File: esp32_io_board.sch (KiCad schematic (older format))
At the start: 59 parts

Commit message: power pins added on txb104
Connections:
- net +3V3: now also U?.14 (VCCB)
- net +5V: now also U?.1 (VCCA)
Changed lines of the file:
@@
 Text Label 7500 3300 0    50   ~ 0
 RESET
+Wire Wire Line
+	6250 4950 6250 4650
+Wire Wire Line
+	6450 4950 6450 4650
+$Comp
+L power:+3.3V #PWR?
+U 1 1 5CB3F95E
+P 6450 4650
+F 0 "#PWR?" H 6450 4500 50  0001 C CNN
+F 1 "+3.3V" H 6465 4823 50  0000 C CNN
+F 2 "" H 6450 4650 50  0001 C CNN
+F 3 "" H 6450 4650 50  0001 C CNN
+	1    6450 4650
+	1    0    0    -1
+$EndComp
+$Comp
+L power:+5V #PWR?
+U 1 1 5CB41F95
+P 6250 4650
+F 0 "#PWR?" H 6250 4500 50  0001 C CNN
+F 1 "+5V" H 6265 4823 50  0000 C CNN
+F 2 "" H 6250 4650 50  0001 C CNN
+F 3 "" H 6250 4650 50  0001 C CNN
+	1    6250 4650
+	1    0    0    -1
+$EndComp
 $EndSCHEMATC

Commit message: cvpcb
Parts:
- C1, C11, C2, C3, C4, C5, C6, C7, C8: renamed from C?; footprint (none) -> Capacitor_SMD:C_0603_1608Metric
- C10: renamed from C?; footprint (none) -> Capacitor_SMD:CP_Elec_4x4.5
- C9: renamed from C?; footprint (none) -> Capacitor_SMD:CP_Elec_4x5.3
- D1: renamed from D?; footprint (none) -> Diode_SMD:D_SOD-123F
- D2: renamed from D?; footprint (none) -> Diode_SMD:D_SOD-323F
- D3, D6, D7: renamed from D?; footprint (none) -> LED_SMD:LED_RGB_5050-6
- D4, D5: renamed from D?; footprint (none) -> LED_SMD:LED_0603_1608Metric
- F1: renamed from F?; footprint (none) -> Fuse:Fuse_1812_4532Metric_Pad1.30x3.40mm_HandSolder
- J1: renamed from J?; footprint (none) -> Connector_USB:USB_Micro-B_Amphenol_10103594-0001LF_Horizontal
- J10, J2: renamed from J?; footprint (none) -> Connector_PinHeader_2.54mm:PinHeader_2x04_P2.54mm_Vertical
- J11, J12, J13, J14, J15, J16, J17, J18, J3, J6, J7, J8, J9: renamed from J?; footprint (none) -> Connector_PinHeader_2.54mm:PinHeader_1x02_P2.54mm_Vertical
- J4: renamed from J?; footprint (none) -> Connector_PinHeader_2.54mm:PinHeader_1x04_P2.54mm_Vertical
- J5: renamed from J?; value Conn_01x02 -> i2c; footprint (none) -> Connector_PinHeader_2.54mm:PinHeader_1x02_P2.54mm_Vertical
- JP1, JP2, JP3: renamed from JP?; footprint (none) -> Jumper:SolderJumper-2_P1.3mm_Open_RoundedPad1.0x1.5mm
- R1, R10, R11, R2, R3, R4, R5, R6, R7, R8, R9: renamed from R?; footprint (none) -> Resistor_SMD:R_0603_1608Metric
- SW1, SW2: renamed from SW?; footprint (none) -> Button_Switch_SMD:SW_SPST_EVPBF
- U5: renamed from U?; footprint (none) -> Package_TO_SOT_SMD:SOT-223
- gave numbers to parts that had none: 5

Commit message: initial layout without traces
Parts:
- D2: footprint Diode_SMD:D_SOD-323F -> Diode_SMD:D_SOD-123F
- D7: footprint LED_SMD:LED_RGB_5050-6 -> LED_SMD:LED_0603_1608Metric
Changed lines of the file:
@@
 F 0 "D2" V 4500 4200 50  0000 L CNN
 F 1 "D_TVS" V 4650 4150 50  0000 L CNN
-F 2 "Diode_SMD:D_SOD-323F" H 4500 4100 50  0001 C CNN
+F 2 "Diode_SMD:D_SOD-123F" H 4500 4100 50  0001 C CNN
 F 3 "~" H 4500 4100 50  0001 C CNN
 	1    4500 4100
@@
 F 0 "D7" H 12792 6445 50  0000 C CNN
 F 1 "LED" H 12792 6536 50  0000 C CNN
-F 2 "LED_SMD:LED_RGB_5050-6" H 12800 6700 50  0001 C CNN
+F 2 "LED_SMD:LED_0603_1608Metric" H 12800 6700 50  0001 C CNN
 F 3 "~" H 12800 6700 50  0001 C CNN
 	1    12800 6700

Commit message: redesign
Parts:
- removed J10: Conn_02x04_Counter_Clockwise, Connector_PinHeader_2.54mm:PinHeader_2x04_P2.54mm_Vertical, symbol Connector_Generic:Conn_02x04_Counter_Clockwise
- removed J5: i2c, Connector_PinHeader_2.54mm:PinHeader_1x02_P2.54mm_Vertical, symbol Connector_Generic:Conn_01x02
- removed J6, J8, J9: Conn_01x02, Connector_PinHeader_2.54mm:PinHeader_1x02_P2.54mm_Vertical, symbol Connector_Generic:Conn_01x02
- added J?: RASPBERRYPI-40-PIN-GPIO, 2X20-SHROUDED, symbol SparkFun-Boards:RASPBERRYPI-40-PIN-GPIO
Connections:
- net GND: now also J?.14 (GND), J?.20 (GND), J?.25 (GND), J?.30 (GND), J?.34 (GND), J?.39 (GND), J?.6 (GND), J?.9 (GND)
- net at U4.21 (SDO): no longer U6.23 (SDA)
- net at U4.22 (SD1): no longer U6.22 (SCL)
- net at U4.23 (IO15): now also U6.23 (SDA)
- net at U4.24 (IO2): now also U6.22 (SCL)
- net rx: now reaches U4.27 (IO16)
- net rx: now also J?.8 (TXO)
- net tx: now reaches U4.28 (IO17)
- net tx: now also J?.10 (RXI)
- net cs: now reaches U4.29 (IO5)
- net cs: now also J?.24 (CE0)
- net clk: now reaches U4.30 (IO18)
- net clk: now also J?.23 (SCLK)
- net miso: now reaches U4.31 (IO19)
- net miso: now also J?.21 (MISO)
- net sda0: now reaches U4.33 (IO21)
- net sda0: now also J?.3 (SDA)
- net scl0: now reaches U4.36 (IO22)
- net scl0: now also J?.5 (SCL)
- net mosi: now reaches U4.37 (IO23)
- net mosi: now also J?.19 (MOSI)
- no-connect marks 14 -> 37
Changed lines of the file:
@@
 Wire Wire Line
 	9150 6950 9150 7100
-$Comp
-L Connector_Generic:Conn_01x02 J6
-U 1 1 5C5742E1
-P 11150 7150
-F 0 "J6" H 11230 7142 50  0000 L CNN
-F 1 "Conn_01x02" H 11230 7051 50  0000 L CNN
-F 2 "Connector_PinHeader_2.54mm:PinHeader_1x02_P2.54mm_Vertical" H 11150 7150 50  0001 C CNN
-F 3 "~" H 11150 7150 50  0001 C CNN
-	1    11150 7150
-	1    0    0    -1
-$EndComp
-$Comp
-L Connector_Generic:Conn_01x02 J5
-U 1 1 5C5EE2B6
-P 9950 8050
-F 0 "J5" V 9823 8130 50  0000 L CNN
-F 1 "i2c" V 10100 7950 50  0000 L CNN
-F 2 "Connector_PinHeader_2.54mm:PinHeader_1x02_P2.54mm_Vertical" H 9950 8050 50  0001 C CNN
-F 3 "~" H 9950 8050 50  0001 C CNN
-	1    9950 8050
-	0    1    1    0
-$EndComp
-Wire Wire Line
-	9850 6950 9850 7850
-Wire Wire Line
-	9950 6950 9950 7850
-Wire Wire Line
-	10250 6950 10250 7850
-Wire Wire Line
-	10350 6950 10350 7750
 Wire Wire Line
 	11000 6450 11000 6550
@@
 	1    0    0    -1
 $EndComp
-Wire Wire Line
-	10350 7750 11500 7750
-Wire Wire Line
-	10250 7850 11500 7850
 Wire Wire Line
 	11500 8750 11250 8750
@@
 $EndComp
 NoConn ~ 10150 6950
-$Comp
-L Connector_Generic:Conn_02x04_Counter_Clockwise J10
-U 1 1 5C5FA466
-P 12400 5750
-F 0 "J10" H 12450 6067 50  0000 C CNN
-F 1 "Conn_02x04_Counter_Clockwise" H 12450 5976 50  0000 C CNN
-F 2 "Connector_PinHeader_2.54mm:PinHeader_2x04_P2.54mm_Vertical" H 12400 5750 50  0001 C CNN
-F 3 "~" H 12400 5750 50  0001 C CNN
-	1    12400 5750
-	1    0    0    -1
-$EndComp
 Wire Wire Line
 	12200 5750 11000 5750
@@
 	11000 5150 12200 5150
 Wire Wire Line
-	12200 5150 12200 5650
-Wire Wire Line
-	12700 5850 12700 5950
-Connection ~ 12700 5950
-Wire Wire Line
-	12700 5950 12700 6100
-Wire Wire Line
-	12700 5750 12700 5650
-Connection ~ 12700 5650
-Wire Wire Line
-	12700 5500 12700 5650
-$Comp
-L power:+3.3V #PWR0133
-U 1 1 5C6D291C
-P 12700 6100
-F 0 "#PWR0133" H 12700 5950 50  0001 C CNN
-F 1 "+3.3V" H 12715 6273 50  0000 C CNN
-F 2 "" H 12700 6100 50  0001 C CNN
-F 3 "" H 12700 6100 50  0001 C CNN
-	1    12700 6100
-	-1   0    0    1
-$EndComp
-$Comp
-L power:GND #PWR0134
-U 1 1 5C6E6494
-P 12700 5500
-F 0 "#PWR0134" H 12700 5250 50  0001 C CNN
-F 1 "GND" V 12705 5372 50  0000 R CNN
-F 2 "" H 12700 5500 50  0001 C CNN
-F 3 "" H 12700 5500 50  0001 C CNN
-	1    12700 5500
-	-1   0    0    1
-$EndComp
-Wire Wire Line
-	10550 6950 10550 7150
-Wire Wire Line
-	10550 7150 10950 7150
-Wire Wire Line
-	10450 6950 10450 7250
-Wire Wire Line
-	10450 7250 10950 7250
-Wire Wire Line
 	11000 6050 11850 6050
 Wire Wire Line
 	11000 6150 11850 6150
-$Comp
-L Connector_Generic:Conn_01x02 J9
-U 1 1 5C73A9E4
-P 12050 6050
-F 0 "J9" H 12130 6042 50  0000 L CNN
-F 1 "Conn_01x02" H 12130 5951 50  0000 L CNN
-F 2 "Connector_PinHeader_2.54mm:PinHeader_1x02_P2.54mm_Vertical" H 12050 6050 50  0001 C CNN
-F 3 "~" H 12050 6050 50  0001 C CNN
-	1    12050 6050
-	1    0    0    -1
-$EndComp
 Wire Wire Line
 	11000 5250 11400 5250
 Wire Wire Line
-	11400 5250 11400 4900
-Wire Wire Line
 	11000 5550 11500 5550
 Wire Wire Line
@@
 Wire Wire Line
 	11000 5450 11900 5450
-$Comp
-L Connector_Generic:Conn_01x02 J8
-U 1 1 5C77D551
-P 11400 4700
-F 0 "J8" H 11480 4692 50  0000 L CNN
-F 1 "Conn_01x02" H 11350 4400 50  0000 L CNN
-F 2 "Connector_PinHeader_2.54mm:PinHeader_1x02_P2.54mm_Vertical" H 11400 4700 50  0001 C CNN
-F 3 "~" H 11400 4700 50  0001 C CNN
-	1    11400 4700
-	0    -1   -1   0
-$EndComp
 Wire Wire Line
 	11000 6250 11200 6250
@@
 	1    0    0    -1
 $EndComp
+$Comp
+L SparkFun-Boards:RASPBERRYPI-40-PIN-GPIO J?
+U 1 1 5C21B215
+P 15050 6350
+F 0 "J?" H 15050 7615 50  0000 C CNN
+F 1 "RASPBERRYPI-40-PIN-GPIO" H 15050 7524 50  0000 C CNN
+F 2 "2X20-SHROUDED" H 15080 6500 20  0001 C CNN
+F 3 "" H 15050 6350 50  0001 C CNN
+	1    15050 6350
+	1    0    0    -1
+$EndComp
+Wire Wire Line
+	15650 5350 16000 5350
+Wire Wire Line
+	15650 5450 16000 5450
+Text Label 16000 5350 0    50   ~ 0
+sda0
+Text Label 16000 5450 0    50   ~ 0
+scl0
+Wire Wire Line
+	14450 6850 14450 6950
+Wire Wire Line
+	14450 7750 14100 7750
+Connection ~ 14450 6950
+Wire Wire Line
+	14450 6950 14450 7050
+Connection ~ 14450 7050
+Wire Wire Line
+	14450 7050 14450 7150
+Connection ~ 14450 7150
+Wire Wire Line
+	14450 7150 14450 7250
+Connection ~ 14450 7250
+Wire Wire Line
+	14450 7250 14450 7350
+Connection ~ 14450 7350
+Wire Wire Line
+	14450 7350 14450 7450
+Connection ~ 14450 7450
+Wire Wire Line
+	14450 7450 14450 7550
+Connection ~ 14450 7550
+Wire Wire Line
+	14450 7550 14450 7750
+$Comp
+L power:GND #PWR?
+U 1 1 5C2B3F61
+P 14100 7750
+F 0 "#PWR?" H 14100 7500 50  0001 C CNN
+F 1 "GND" V 14105 7622 50  0000 R CNN
+F 2 "" H 14100 7750 50  0001 C CNN
+F 3 "" H 14100 7750 50  0001 C CNN
+	1    14100 7750
+	0    1    1    0
+$EndComp
+Wire Wire Line
+	11400 5250 11400 4900
+Text Label 11400 4900 1    50   ~ 0
+scl0
+Text Label 11500 4900 1    50   ~ 0
+sda0
+Wire Wire Line
+	10450 7850 11500 7850
+Wire Wire Line
+	10450 6950 10450 7850
+Wire Wire Line
+	10550 6950 10550 7750
+Wire Wire Line
+	10550 7750 11500 7750
+Text Label 11850 6050 0    50   ~ 0
+tx
+Text Label 11850 6150 0    50   ~ 0
+rx
+Wire Wire Line
+	15650 5650 16000 5650
+Wire Wire Line
+	15650 5750 16000 5750
+Text Label 16000 5650 0    50   ~ 0
+rx
+Text Label 16000 5750 0    50   ~ 0
+tx
+Text Label 12200 5150 0    50   ~ 0
+mosi
+Text Label 12200 5750 0    50   ~ 0
+miso
+Text Label 12200 5850 0    50   ~ 0
+clk
+Text Label 12200 5950 0    50   ~ 0
+cs
+Text Label 16000 5950 0    50   ~ 0
+clk
+Wire Wire Line
+	15650 5950 16000 5950
+Wire Wire Line
+	15650 6050 16000 6050
+Wire Wire Line
+	15650 6150 16000 6150
+Wire Wire Line
+	15650 6250 16000 6250
+Text Label 16000 6050 0    50   ~ 0
+miso
+Text Label 16000 6150 0    50   ~ 0
+mosi
+Text Label 16000 6250 0    50   ~ 0
+cs
+NoConn ~ 14450 5850
+NoConn ~ 14450 5950
+NoConn ~ 14450 6050
+NoConn ~ 14450 6150
+NoConn ~ 14450 6250
+NoConn ~ 14450 6350
+NoConn ~ 14450 6450
+NoConn ~ 14450 6550
+NoConn ~ 14450 6650
+NoConn ~ 15650 6550
+NoConn ~ 15650 6650
+NoConn ~ 15650 6750
+NoConn ~ 15650 6850
+NoConn ~ 15650 6950
+NoConn ~ 15650 7050
+NoConn ~ 15650 7150
+NoConn ~ 15650 7250
+NoConn ~ 15650 7450
+NoConn ~ 15650 7550
+NoConn ~ 9950 6950
+NoConn ~ 10250 6950
+NoConn ~ 10350 6950
+NoConn ~ 9850 6950
 $EndSCHEMATC

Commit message: annotation
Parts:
- added D8: DIODESOD-123, Diode_SMD:D_SOD-123F, symbol adafruit:DIODESOD-123
- added H1, H2, H3, H4, H5, H6: MountingHole, MountingHole:MountingHole_3mm, symbol Mechanical:MountingHole
- J5: renamed from J?; footprint 2X20-SHROUDED -> SparkFun-Boards:2X20-SHROUDED
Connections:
- net +3V3: now also D8.A
- net at J5.1 (3.3V): now also J5.17 (3.3V), D8.C
- no-connect marks 37 -> 39
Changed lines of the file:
@@
 $EndComp
 $Comp
-L SparkFun-Boards:RASPBERRYPI-40-PIN-GPIO J?
+L SparkFun-Boards:RASPBERRYPI-40-PIN-GPIO J5
 U 1 1 5C21B215
 P 15050 6350
-F 0 "J?" H 15050 7615 50  0000 C CNN
+F 0 "J5" H 15050 7615 50  0000 C CNN
 F 1 "RASPBERRYPI-40-PIN-GPIO" H 15050 7524 50  0000 C CNN
-F 2 "2X20-SHROUDED" H 15080 6500 20  0001 C CNN
+F 2 "SparkFun-Boards:2X20-SHROUDED" H 15080 6500 20  0001 C CNN
 F 3 "" H 15050 6350 50  0001 C CNN
 	1    15050 6350
@@
 	14450 7550 14450 7750
 $Comp
-L power:GND #PWR?
+L power:GND #PWR0133
 U 1 1 5C2B3F61
 P 14100 7750
-F 0 "#PWR?" H 14100 7500 50  0001 C CNN
+F 0 "#PWR0133" H 14100 7500 50  0001 C CNN
 F 1 "GND" V 14105 7622 50  0000 R CNN
 F 2 "" H 14100 7750 50  0001 C CNN
@@
 NoConn ~ 10350 6950
 NoConn ~ 9850 6950
+NoConn ~ 14450 5350
+NoConn ~ 14450 5450
+Wire Wire Line
+	14450 5550 14350 5550
+Wire Wire Line
+	14450 5650 14350 5650
+Wire Wire Line
+	14350 5650 14350 5550
+Connection ~ 14350 5550
+Wire Wire Line
+	14350 5550 14000 5550
+$Comp
+L adafruit:DIODESOD-123 D8
+U 1 1 5C5AD2D7
+P 13900 5550
+F 0 "D8" H 13900 5765 50  0000 C CNN
+F 1 "DIODESOD-123" H 13900 5674 50  0000 C CNN
+F 2 "Diode_SMD:D_SOD-123F" H 13930 5700 20  0001 C CNN
+F 3 "" H 13900 5550 50  0001 C CNN
+	1    13900 5550
+	1    0    0    -1
+$EndComp
+Wire Wire Line
+	13800 5550 13550 5550
+$Comp
+L power:+3.3V #PWR0134
+U 1 1 5C5CAF79
+P 13550 5550
+F 0 "#PWR0134" H 13550 5400 50  0001 C CNN
+F 1 "+3.3V" V 13565 5678 50  0000 L CNN
+F 2 "" H 13550 5550 50  0001 C CNN
+F 3 "" H 13550 5550 50  0001 C CNN
+	1    13550 5550
+	0    -1   -1   0
+$EndComp
+$Comp
+L Mechanical:MountingHole H4
+U 1 1 5C6145C5
+P 14450 8200
+F 0 "H4" H 14550 8246 50  0000 L CNN
+F 1 "MountingHole" H 14550 8155 50  0000 L CNN
+F 2 "MountingHole:MountingHole_3mm" H 14450 8200 50  0001 C CNN
+F 3 "~" H 14450 8200 50  0001 C CNN
+	1    14450 8200
+	1    0    0    -1
+$EndComp
+$Comp
+L Mechanical:MountingHole H5
+U 1 1 5C6146C1
+P 14450 8400
+F 0 "H5" H 14550 8446 50  0000 L CNN
+F 1 "MountingHole" H 14550 8355 50  0000 L CNN
+F 2 "MountingHole:MountingHole_3mm" H 14450 8400 50  0001 C CNN
+F 3 "~" H 14450 8400 50  0001 C CNN
+	1    14450 8400
+	1    0    0    -1
+$EndComp
+$Comp
+L Mechanical:MountingHole H1
+U 1 1 5C614951
+P 14250 8200
+F 0 "H1" H 14350 8246 50  0000 L CNN
+F 1 "MountingHole" H 14350 8155 50  0000 L CNN
+F 2 "MountingHole:MountingHole_3mm" H 14250 8200 50  0001 C CNN
+F 3 "~" H 14250 8200 50  0001 C CNN
+	1    14250 8200
+	1    0    0    -1
+$EndComp
+$Comp
+L Mechanical:MountingHole H2
+U 1 1 5C614BA5
+P 14250 8400
+F 0 "H2" H 14350 8446 50  0000 L CNN
+F 1 "MountingHole" H 14350 8355 50  0000 L CNN
+F 2 "MountingHole:MountingHole_3mm" H 14250 8400 50  0001 C CNN
+F 3 "~" H 14250 8400 50  0001 C CNN
+	1    14250 8400
+	1    0    0    -1
+$EndComp
+$Comp
+L Mechanical:MountingHole H3
+U 1 1 5C614C31
+P 14250 8600
+F 0 "H3" H 14350 8646 50  0000 L CNN
+F 1 "MountingHole" H 14350 8555 50  0000 L CNN
+F 2 "MountingHole:MountingHole_3mm" H 14250 8600 50  0001 C CNN
+F 3 "~" H 14250 8600 50  0001 C CNN
+	1    14250 8600
+	1    0    0    -1
+$EndComp
+$Comp
+L Mechanical:MountingHole H6
+U 1 1 5C614CBF
+P 14450 8600
+F 0 "H6" H 14550 8646 50  0000 L CNN
+F 1 "MountingHole" H 14550 8555 50  0000 L CNN
+F 2 "MountingHole:MountingHole_3mm" H 14450 8600 50  0001 C CNN
+F 3 "~" H 14450 8600 50  0001 C CNN
+	1    14450 8600
+	1    0    0    -1
+$EndComp
 $EndSCHEMATC

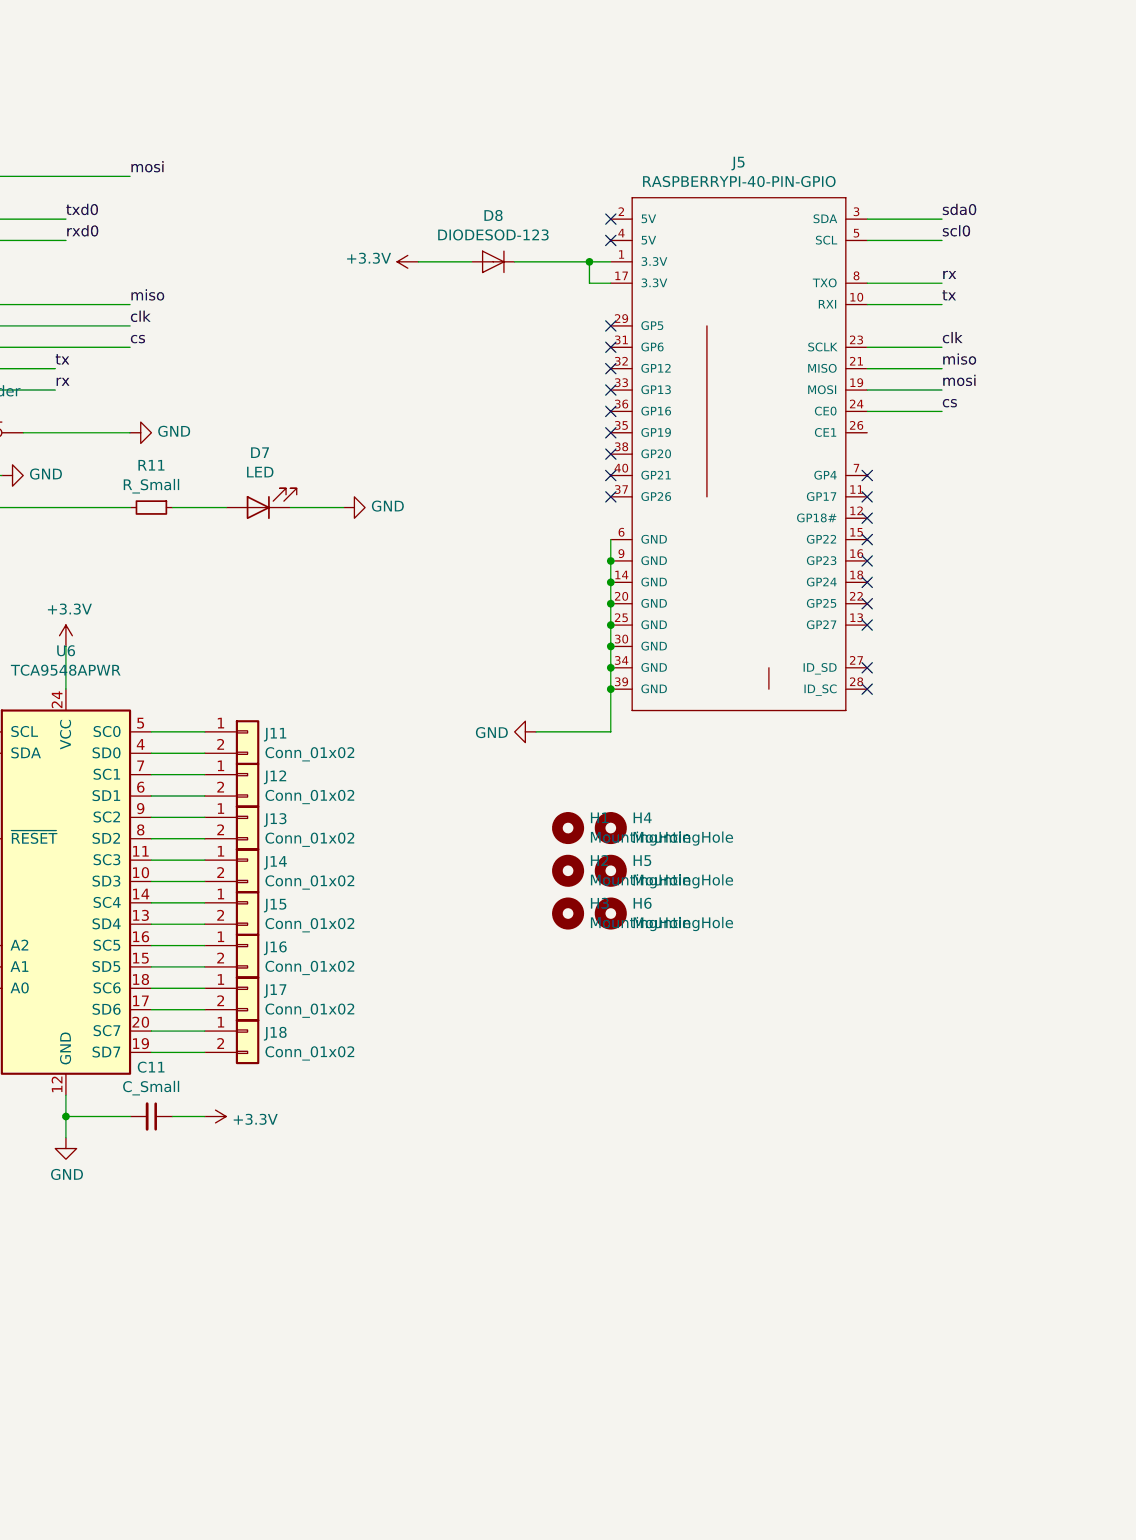
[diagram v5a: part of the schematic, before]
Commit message: raspberry pi integration
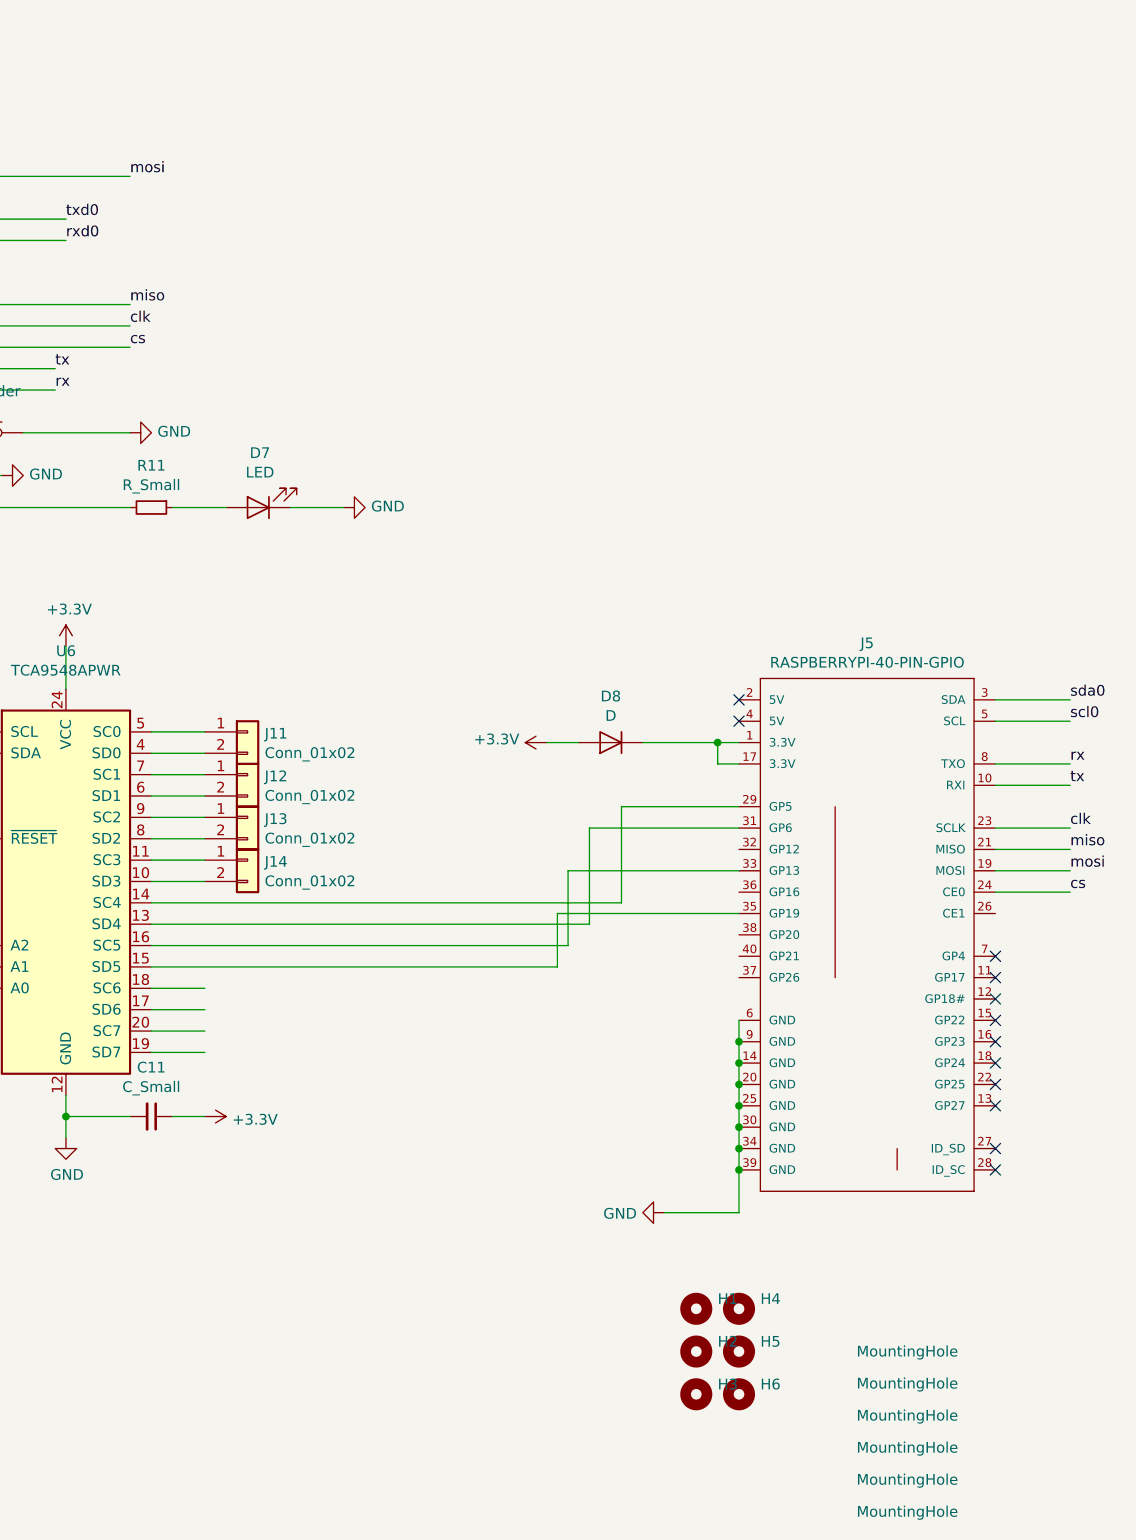
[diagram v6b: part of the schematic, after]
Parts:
- removed D8: DIODESOD-123, Diode_SMD:D_SOD-123F, symbol adafruit:DIODESOD-123
- removed J15, J16, J17, J18: Conn_01x02, Connector_PinHeader_2.54mm:PinHeader_1x02_P2.54mm_Vertical, symbol Connector_Generic:Conn_01x02
- added D8: D, Diode_SMD:D_SOD-123F, symbol Device:D
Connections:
- net +3V3: now also D8.2 (A)
- net at J5.1 (3.3V), J5.17 (3.3V): now also D8.1 (K)
- net at J5.29 (GP5): now also U6.14 (SC4)
- net at J5.31 (GP6): now also U6.13 (SD4)
- net at J5.33 (GP13): now also U6.16 (SC5)
- net at J5.35 (GP19): now also U6.15 (SD5)
- no-connect marks 39 -> 30
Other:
- moved on the sheet: H1, H2, H3, H4, H5, H6, J5
